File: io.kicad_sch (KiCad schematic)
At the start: 16 parts, among them J17 FTDI, J18 A10, J19 A5-1, J20 A5-2, J21 A2-1, J22 A2-2, J23 A2-3, J24 A2-4, J25 A2-5, J28 D8, J29 D4-1, J30 D4-2, J31 D2-1, J32 D2-2, J33 D2-3, J34 D2-4

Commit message: Add an FTDI connector for the DALI bus
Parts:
- added J35: FTDI-DALI, symbol Connector:Conn_01x06_Pin
- J17: value FTDI -> FTDI-MCU
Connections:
- net GND: now also J35.1 (Pin_1)
- net FTDI_RXD renamed FTDI_MCU_RXD
- net FTDI_TXD renamed FTDI_MCU_TXD
- new net FTDI_DALI_RXD: J35.5 (Pin_5)
- new net FTDI_DALI_TXD: J35.4 (Pin_4)
- no-connect marks 3 -> 6
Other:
- moved on the sheet: J17
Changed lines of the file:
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@@
 	(generator "eeschema")
 	(generator_version "9.0")
-	(paper "User" 205 95)
+	(paper "User" 210 95)
 	(no_connect
-		(at 187.96 66.04)
+		(at 187.96 73.66)
+	)
+	(no_connect
+		(at 187.96 39.37)
+	)
+	(no_connect
+		(at 187.96 36.83)
 	)
 	(no_connect
@@
 	)
 	(no_connect
-		(at 187.96 73.66)
+		(at 187.96 46.99)
+	)
+	(no_connect
+		(at 187.96 66.04)
+	)
+	(hierarchical_label "FTDI_DALI_TXD"
+		(shape bidirectional)
+		(at 187.96 68.58 0)
+		(effects
+			(font
+				(size 1.27 1.27)
+			)
+			(justify left)
+		)
 	)
 	(hierarchical_label "IO_A9"
@@
 		)
 	)
-	(hierarchical_label "FTDI_RXD"
+	(hierarchical_label "FTDI_MCU_RXD"
 		(shape bidirectional)
-		(at 187.96 71.12 0)
+		(at 187.96 44.45 0)
 		(effects
 			(font
@@
 		)
 	)
+	(hierarchical_label "FTDI_DALI_RXD"
+		(shape bidirectional)
+		(at 187.96 71.12 0)
+		(effects
+			(font
+				(size 1.27 1.27)
+			)
+			(justify left)
+		)
+	)
 	(hierarchical_label "IO_A1"
 		(shape bidirectional)
@@
 		)
 	)
-	(hierarchical_label "FTDI_TXD"
+	(hierarchical_label "FTDI_MCU_TXD"
 		(shape bidirectional)
-		(at 187.96 68.58 0)
+		(at 187.96 41.91 0)
 		(effects
 			(font
@@
 	)
 	(symbol
+		(lib_id "power:GND")
+		(at 187.96 60.96 90)
+		(unit 1)
+		(exclude_from_sim no)
+		(in_bom yes)
+		(on_board yes)
+		(dnp no)
+		(fields_autoplaced yes)
+		(property "Reference" "#PWR083"
+			(at 194.31 60.96 0)
+			(effects
+				(font
+					(size 1.27 1.27)
+				)
+				(hide yes)
+			)
+		)
+		(property "Value" "GND"
+			(at 191.77 60.9599 90)
+			(effects
+				(font
+					(size 1.27 1.27)
+				)
+				(justify right)
+			)
+		)
+		(property "Footprint" ""
+			(at 187.96 60.96 0)
+			(effects
+				(font
+					(size 1.27 1.27)
+				)
+				(hide yes)
+			)
+		)
+		(property "Datasheet" ""
+			(at 187.96 60.96 0)
+			(effects
+				(font
+					(size 1.27 1.27)
+				)
+				(hide yes)
+			)
+		)
+		(property "Description" "Power symbol creates a global label with name \"GND\" , ground"
+			(at 187.96 60.96 0)
+			(effects
+				(font
+					(size 1.27 1.27)
+				)
+				(hide yes)
+			)
+		)
+		(pin "1"
+		)
+		(instances
+			(project "dali-pcb"
+				(path "/aa7f7e07-1f39-4222-a272-c9975d033b6d/6cac1b53-24ad-4dc9-955d-941983abac95"
+					(reference "#PWR083")
+					(unit 1)
+				)
+			)
+		)
+	)
+	(symbol
 		(lib_id "power:+5V")
 		(at 86.36 60.96 270)
@@
 	(symbol
 		(lib_id "power:GND")
-		(at 187.96 60.96 90)
+		(at 187.96 34.29 90)
 		(unit 1)
 		(exclude_from_sim no)
@@
 		(fields_autoplaced yes)
 		(property "Reference" "#PWR037"
-			(at 194.31 60.96 0)
+			(at 194.31 34.29 0)
 			(effects
 				(font
@@
 		)
 		(property "Value" "GND"
-			(at 191.77 60.9599 90)
+			(at 191.77 34.2899 90)
 			(effects
 				(font
@@
 		)
 		(property "Footprint" ""
-			(at 187.96 60.96 0)
+			(at 187.96 34.29 0)
 			(effects
 				(font
@@
 		)
 		(property "Datasheet" ""
-			(at 187.96 60.96 0)
+			(at 187.96 34.29 0)
 			(effects
 				(font
@@
 		)
 		(property "Description" "Power symbol creates a global label with name \"GND\" , ground"
-			(at 187.96 60.96 0)
+			(at 187.96 34.29 0)
 			(effects
 				(font
@@
 	(symbol
 		(lib_id "Connector:Conn_01x06_Pin")
-		(at 182.88 66.04 0)
+		(at 182.88 39.37 0)
 		(unit 1)
 		(exclude_from_sim no)
@@
 		(fields_autoplaced yes)
 		(property "Reference" "J17"
-			(at 183.515 55.88 0)
+			(at 183.515 29.21 0)
 			(effects
 				(font
@@
 			)
 		)
-		(property "Value" "FTDI"
-			(at 183.515 58.42 0)
+		(property "Value" "FTDI-MCU"
+			(at 183.515 31.75 0)
 			(effects
 				(font
@@
 		)
 		(property "Footprint" ""
-			(at 182.88 66.04 0)
+			(at 182.88 39.37 0)
 			(effects
 				(font
@@
 		)
 		(property "Datasheet" "~"
-			(at 182.88 66.04 0)
+			(at 182.88 39.37 0)
 			(effects
 				(font
@@
 		)
 		(property "Description" "Generic connector, single row, 01x06, script generated"
-			(at 182.88 66.04 0)
+			(at 182.88 39.37 0)
 			(effects
 				(font
@@
 					(unit 1)
 				)
+			)
+		)
+	)
+	(symbol
+		(lib_id "Connector:Conn_01x06_Pin")
+		(at 182.88 66.04 0)
+		(unit 1)
+		(exclude_from_sim no)
+		(in_bom yes)
+		(on_board yes)
+		(dnp no)
+		(property "Reference" "J35"
+			(at 183.515 55.88 0)
+			(effects
+				(font
+					(size 1.27 1.27)
+				)
+			)
+		)
+		(property "Value" "FTDI-DALI"
+			(at 183.515 58.42 0)
+			(effects
+				(font
+					(size 1.27 1.27)
+				)
+			)
+		)
+		(property "Footprint" ""
+			(at 182.88 66.04 0)
+			(effects
+				(font
+					(size 1.27 1.27)
+				)
+				(hide yes)
+			)
+		)
+		(property "Datasheet" "~"
+			(at 182.88 66.04 0)
+			(effects
+				(font
+					(size 1.27 1.27)
+				)
+				(hide yes)
+			)
+		)
+		(property "Description" "Generic connector, single row, 01x06, script generated"
+			(at 182.88 66.04 0)
+			(effects
+				(font
+					(size 1.27 1.27)
+				)
+				(hide yes)
+			)
+		)
+		(pin "2"
+		)
+		(pin "4"
+		)
+		(pin "5"
+		)
+		(pin "6"
+		)
+		(pin "1"
+		)
+		(pin "3"
+		)
+		(instances
+			(project "dali-pcb"
+				(path "/aa7f7e07-1f39-4222-a272-c9975d033b6d/6cac1b53-24ad-4dc9-955d-941983abac95"
+					(reference "J35")
+					(unit 1)
+				)

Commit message: Connect 5V from the FTDI connector to the DALI comms circuit
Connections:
- net +5V: now also J35.3 (Pin_3)
- no-connect marks 6 -> 5
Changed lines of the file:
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@@
 		(at 187.96 46.99)
-	)
-	(no_connect
-		(at 187.96 66.04)
 	)
 	(hierarchical_label "FTDI_DALI_TXD"
@@
 					(unit 1)
 				)
+			)
+		)
+	)
+	(symbol
+		(lib_id "power:+5V")
+		(at 187.96 66.04 270)
+		(unit 1)
+		(exclude_from_sim no)
+		(in_bom yes)
+		(on_board yes)
+		(dnp no)
+		(fields_autoplaced yes)
+		(property "Reference" "#PWR084"
+			(at 184.15 66.04 0)
+			(effects
+				(font
+					(size 1.27 1.27)
+				)
+				(hide yes)
+			)
+		)
+		(property "Value" "+5V"
+			(at 191.77 66.0399 90)
+			(effects
+				(font
+					(size 1.27 1.27)
+				)
+				(justify left)
+			)
+		)
+		(property "Footprint" ""
+			(at 187.96 66.04 0)
+			(effects
+				(font
+					(size 1.27 1.27)
+				)
+				(hide yes)
+			)
+		)
+		(property "Datasheet" ""
+			(at 187.96 66.04 0)
+			(effects
+				(font
+					(size 1.27 1.27)
+				)
+				(hide yes)
+			)
+		)
+		(property "Description" "Power symbol creates a global label with name \"+5V\""
+			(at 187.96 66.04 0)
+			(effects
+				(font
+					(size 1.27 1.27)
+				)
+				(hide yes)
+			)
+		)
+		(pin "1"
+		)
+		(instances
+			(project "dali-pcb"
+				(path "/aa7f7e07-1f39-4222-a272-c9975d033b6d/6cac1b53-24ad-4dc9-955d-941983abac95"
+					(reference "#PWR084")
+					(unit 1)
+				)

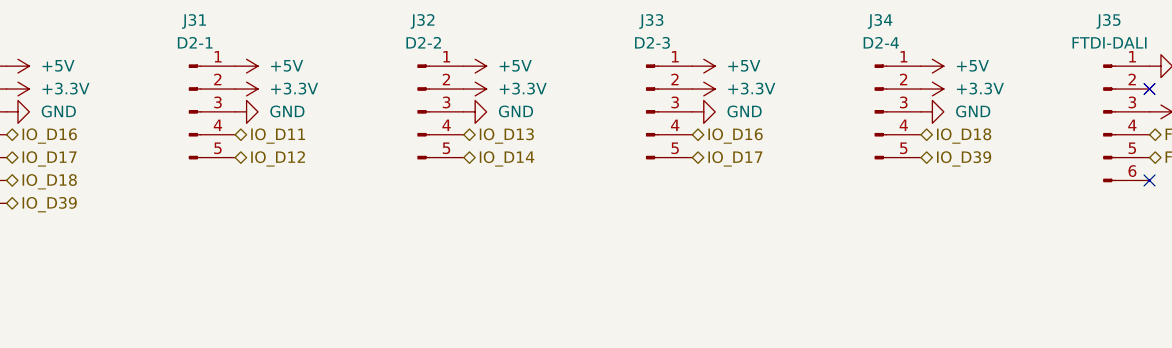
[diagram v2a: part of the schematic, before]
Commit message: Add individual two-pin switch I/O headers
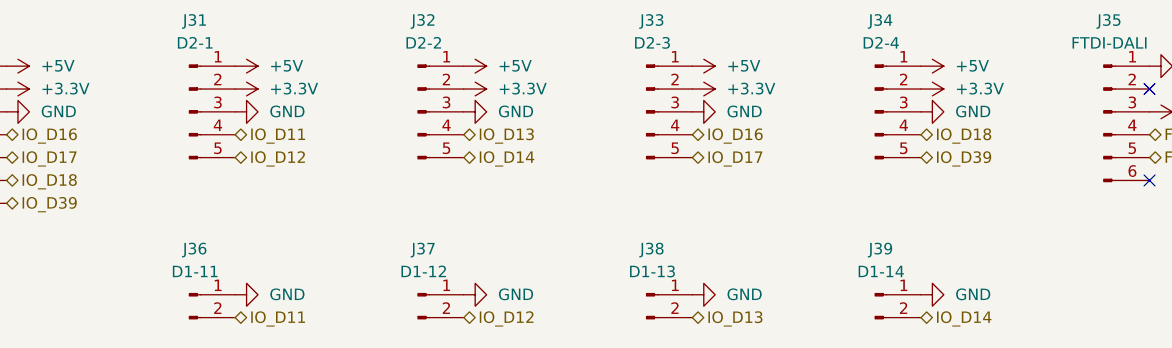
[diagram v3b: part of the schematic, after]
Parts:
- added J36: D1-11, symbol Connector:Conn_01x02_Pin
- added J37: D1-12, symbol Connector:Conn_01x02_Pin
- added J38: D1-13, symbol Connector:Conn_01x02_Pin
- added J39: D1-14, symbol Connector:Conn_01x02_Pin
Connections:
- net GND: now also J36.1 (Pin_1), J37.1 (Pin_1), J38.1 (Pin_1), J39.1 (Pin_1)
- net IO_D11: now also J36.2 (Pin_2)
- net IO_D12: now also J37.2 (Pin_2)
- net IO_D13: now also J38.2 (Pin_2)
- net IO_D14: now also J39.2 (Pin_2)

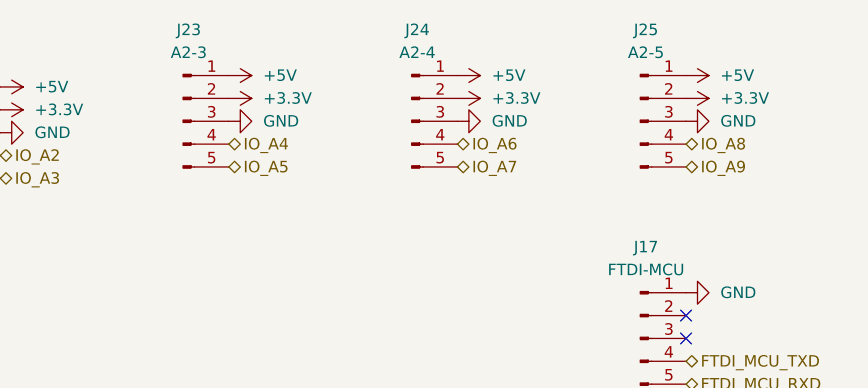
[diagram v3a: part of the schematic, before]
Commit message: Assign footprints for the remaining components
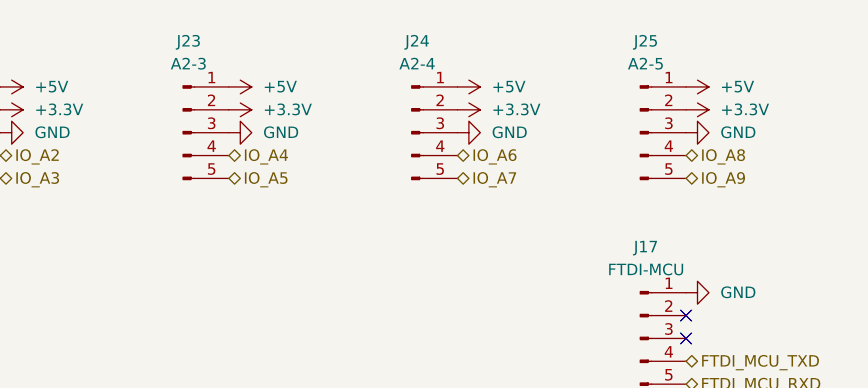
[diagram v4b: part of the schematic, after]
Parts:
- J17, J35: footprint (none) -> Connector_PinHeader_2.54mm:PinHeader_1x06_P2.54mm_Vertical
- J18: footprint (none) -> Connector_PinHeader_2.54mm:PinHeader_1x13_P2.54mm_Vertical
- J19, J20: footprint (none) -> Connector_PinHeader_2.54mm:PinHeader_1x08_P2.54mm_Vertical
- J21, J22, J23, J24, J25, J31, J32, J33, J34: footprint (none) -> Connector_PinHeader_2.54mm:PinHeader_1x05_P2.54mm_Vertical
- J28: footprint (none) -> Connector_PinHeader_2.54mm:PinHeader_1x11_P2.54mm_Vertical
- J29, J30: footprint (none) -> Connector_PinHeader_2.54mm:PinHeader_1x07_P2.54mm_Vertical
- J36, J37, J38, J39: footprint (none) -> Connector_PinHeader_2.54mm:PinHeader_1x02_P2.54mm_Vertical
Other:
- moved on the sheet: J23, J24, J25

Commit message: Place all components
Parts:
- renumbered J28 to J26, J29 to J27, J30 to J28, J31 to J29, J32 to J30, J33 to J31, J34 to J32, J36 to J33, J37 to J34, J38 to J35, J39 to J36, J35 to J37
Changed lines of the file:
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@@
 		(dnp no)
 		(fields_autoplaced yes)
-		(property "Reference" "J31"
+		(property "Reference" "J29"
 			(at 81.915 55.88 0)
 			(effects
@@
 			(project "dali-pcb"
 				(path "/aa7f7e07-1f39-4222-a272-c9975d033b6d/6cac1b53-24ad-4dc9-955d-941983abac95"
-					(reference "J31")
+					(reference "J29")
 					(unit 1)
 				)
@@
 		(dnp no)
 		(fields_autoplaced yes)
-		(property "Reference" "J32"
+		(property "Reference" "J30"
 			(at 107.315 55.88 0)
 			(effects
@@
 			(project "dali-pcb"
 				(path "/aa7f7e07-1f39-4222-a272-c9975d033b6d/6cac1b53-24ad-4dc9-955d-941983abac95"
-					(reference "J32")
+					(reference "J30")
 					(unit 1)
 				)
@@
 		(dnp no)
 		(fields_autoplaced yes)
-		(property "Reference" "J38"
+		(property "Reference" "J35"
 			(at 132.715 81.28 0)
 			(effects
@@
 			(project "dali-pcb"
 				(path "/aa7f7e07-1f39-4222-a272-c9975d033b6d/6cac1b53-24ad-4dc9-955d-941983abac95"
-					(reference "J38")
+					(reference "J35")
 					(unit 1)
 				)
@@
 		(dnp no)
 		(fields_autoplaced yes)
-		(property "Reference" "J36"
+		(property "Reference" "J33"
 			(at 81.915 81.28 0)
 			(effects
@@
 			(project "dali-pcb"
 				(path "/aa7f7e07-1f39-4222-a272-c9975d033b6d/6cac1b53-24ad-4dc9-955d-941983abac95"
-					(reference "J36")
+					(reference "J33")
 					(unit 1)
 				)
@@
 		(dnp no)
 		(fields_autoplaced yes)
-		(property "Reference" "J30"
+		(property "Reference" "J28"
 			(at 56.515 55.88 0)
 			(effects
@@
 			(project "dali-pcb"
 				(path "/aa7f7e07-1f39-4222-a272-c9975d033b6d/6cac1b53-24ad-4dc9-955d-941983abac95"
-					(reference "J30")
+					(reference "J28")
 					(unit 1)
 				)
@@
 		(dnp no)
 		(fields_autoplaced yes)
-		(property "Reference" "J33"
+		(property "Reference" "J31"
 			(at 132.715 55.88 0)
 			(effects
@@
 			(project "dali-pcb"
 				(path "/aa7f7e07-1f39-4222-a272-c9975d033b6d/6cac1b53-24ad-4dc9-955d-941983abac95"
-					(reference "J33")
+					(reference "J31")
 					(unit 1)
 				)
@@
 		(dnp no)
 		(fields_autoplaced yes)
-		(property "Reference" "J28"
+		(property "Reference" "J26"
 			(at 5.715 55.88 0)
 			(effects
@@
 			(project ""
 				(path "/aa7f7e07-1f39-4222-a272-c9975d033b6d/6cac1b53-24ad-4dc9-955d-941983abac95"
-					(reference "J28")
+					(reference "J26")
 					(unit 1)
 				)
@@
 		(dnp no)
 		(fields_autoplaced yes)
-		(property "Reference" "J29"
+		(property "Reference" "J27"
 			(at 32.385 55.88 0)
 			(effects
@@
 			(project "dali-pcb"
 				(path "/aa7f7e07-1f39-4222-a272-c9975d033b6d/6cac1b53-24ad-4dc9-955d-941983abac95"
-					(reference "J29")
+					(reference "J27")
 					(unit 1)
 				)
@@
 		(dnp no)
 		(fields_autoplaced yes)
-		(property "Reference" "J34"
+		(property "Reference" "J32"
 			(at 158.115 55.88 0)
 			(effects
@@
 			(project "dali-pcb"
 				(path "/aa7f7e07-1f39-4222-a272-c9975d033b6d/6cac1b53-24ad-4dc9-955d-941983abac95"
-					(reference "J34")
+					(reference "J32")
 					(unit 1)
 				)
@@
 		(dnp no)
 		(fields_autoplaced yes)
-		(property "Reference" "J39"
+		(property "Reference" "J36"
 			(at 158.115 81.28 0)
 			(effects
@@
 			(project "dali-pcb"
 				(path "/aa7f7e07-1f39-4222-a272-c9975d033b6d/6cac1b53-24ad-4dc9-955d-941983abac95"
-					(reference "J39")
+					(reference "J36")
 					(unit 1)
 				)
@@
 		(dnp no)
 		(fields_autoplaced yes)
-		(property "Reference" "J37"
+		(property "Reference" "J34"
 			(at 107.315 81.28 0)
 			(effects
@@
 			(project "dali-pcb"
 				(path "/aa7f7e07-1f39-4222-a272-c9975d033b6d/6cac1b53-24ad-4dc9-955d-941983abac95"
-					(reference "J37")
+					(reference "J34")
 					(unit 1)
 				)
@@
 		(on_board yes)
 		(dnp no)
-		(property "Reference" "J35"
+		(property "Reference" "J37"
 			(at 183.515 55.88 0)
 			(effects
@@
 			(project "dali-pcb"
 				(path "/aa7f7e07-1f39-4222-a272-c9975d033b6d/6cac1b53-24ad-4dc9-955d-941983abac95"
-					(reference "J35")
+					(reference "J37")
 					(unit 1)
 				)
